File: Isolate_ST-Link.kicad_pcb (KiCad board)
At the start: 2 copper layers, 39 x 38 mm, 70 parts, among them J1 USB_OTG, J2 CONN_01X06, J3 CONN_01X04, J4 CONN_01X02, J5 CONN_01X02, J6 GS2, Q1 BSS138, U1 MAU10x, U2 ADuM4160, U3 APE8865NR-33-HF-3, U4 STM32F103CBTx, Y1 Crystal

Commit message: 進捗
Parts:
- moved R30 0.10 mm to (166.1, 75.4)
- moved R31 0.10 mm to (161.6, 75.4)
- moved R32 0.10 mm to (163.1, 75.4)
- moved R33 0.10 mm to (164.6, 75.4)
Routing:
- net GND: track 336.2 -> 383.5 mm, vias 93 -> 114
- net +3V3: track 138.4 -> 124.2 mm, vias 9 -> 8
- net /MCU/Vtarget: track 18.6 -> 20.7 mm
- net Net-(J2-Pad4): track 7.32 -> 8.08 mm
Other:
- board text added: "Vtgt"

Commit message: 進捗
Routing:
- net GND: track 383.5 -> 446.4 mm, vias 114 -> 137
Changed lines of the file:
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@@
-(kicad_pcb (version 4) (host pcbnew 4.0.7)
+(kicad_pcb (version 4) (host pcbnew 4.0.6)
   (general
     (links 148)
@@
     (thickness 1.6)
     (drawings 49)
-    (tracks 1041)
+    (tracks 1094)
     (zones 0)
     (modules 70)
@@
     (pad_to_mask_clearance 0)
     (aux_axis_origin 0 0)
-    (grid_origin 193 50)
     (visible_elements 7FFFFFFF)
     (pcbplotparams
@@
     (tags D_SOD-123F)
     (attr smd)
-    (fp_text reference D9 (at -3.3 0.1 90) (layer B.SilkS)
+    (fp_text reference D9 (at -3.2 0 90) (layer B.SilkS)
       (effects (font (size 1 1) (thickness 0.15)) (justify mirror))
     )
@@
     (tags "resistor 0603")
     (attr smd)
-    (fp_text reference R21 (at 2.6 0 180) (layer B.SilkS)
+    (fp_text reference R21 (at 0 1.4 180) (layer B.SilkS)
       (effects (font (size 1 1) (thickness 0.15)) (justify mirror))
     )
@@
     (tags "resistor 0603")
     (attr smd)
-    (fp_text reference R23 (at 0.2 -1.3 180) (layer B.SilkS)
+    (fp_text reference R23 (at -0.45 1.35 180) (layer B.SilkS)
       (effects (font (size 1 1) (thickness 0.15)) (justify mirror))
     )
@@
     (tags "resistor 0603")
     (attr smd)
-    (fp_text reference R25 (at 0 -1.4 180) (layer B.SilkS)
+    (fp_text reference R25 (at -0.15 -1.45 180) (layer B.SilkS)
       (effects (font (size 1 1) (thickness 0.15)) (justify mirror))
     )
@@
   (segment (start 163.075 60.95) (end 163.735 60.29) (width 0.6) (layer F.Cu) (net 3))
   (segment (start 163.735 60.29) (end 165.325001 60.29) (width 0.6) (layer F.Cu) (net 3))
+  (segment (start 185.8 57.3) (end 187.7 59.2) (width 0.25) (layer F.Cu) (net 4))
+  (segment (start 187.7 59.2) (end 187.8 59.2) (width 0.25) (layer F.Cu) (net 4))
+  (via (at 187.8 59.2) (size 0.6) (drill 0.4) (layers F.Cu B.Cu) (net 4))
+  (segment (start 185.8 57.3) (end 187.7 57.3) (width 0.25) (layer B.Cu) (net 4))
+  (segment (start 187.7 57.3) (end 187.8 57.2) (width 0.25) (layer B.Cu) (net 4))
+  (via (at 187.8 57.2) (size 0.6) (drill 0.4) (layers F.Cu B.Cu) (net 4))
+  (segment (start 185.8 57.3) (end 187.5 55.6) (width 0.25) (layer F.Cu) (net 4))
+  (segment (start 187.5 55.6) (end 187.8 55.6) (width 0.25) (layer F.Cu) (net 4))
+  (via (at 187.8 55.6) (size 0.6) (drill 0.4) (layers F.Cu B.Cu) (net 4))
+  (segment (start 185.8 57.3) (end 185.8 59.2) (width 0.25) (layer B.Cu) (net 4))
+  (via (at 185.8 59.2) (size 0.6) (drill 0.4) (layers F.Cu B.Cu) (net 4))
+  (segment (start 183.6 55.6) (end 181 55.6) (width 0.25) (layer F.Cu) (net 4))
+  (via (at 181 55.6) (size 0.6) (drill 0.4) (layers F.Cu B.Cu) (net 4))
+  (segment (start 185.8 57.3) (end 183.9 59.2) (width 0.25) (layer F.Cu) (net 4))
+  (segment (start 183.9 59.2) (end 183.6 59.2) (width 0.25) (layer F.Cu) (net 4))
+  (via (at 183.6 59.2) (size 0.6) (drill 0.4) (layers F.Cu B.Cu) (net 4))
+  (segment (start 185.8 57.3) (end 184.1 55.6) (width 0.25) (layer F.Cu) (net 4))
+  (segment (start 184.1 55.6) (end 183.6 55.6) (width 0.25) (layer F.Cu) (net 4))
+  (via (at 183.6 55.6) (size 0.6) (drill 0.4) (layers F.Cu B.Cu) (net 4))
+  (segment (start 157 75.4) (end 154.2 75.4) (width 0.25) (layer F.Cu) (net 4))
+  (via (at 154.2 75.4) (size 0.6) (drill 0.4) (layers F.Cu B.Cu) (net 4))
+  (segment (start 157 77.2) (end 154.2 77.2) (width 0.25) (layer B.Cu) (net 4))
+  (via (at 154.2 77.2) (size 0.6) (drill 0.4) (layers F.Cu B.Cu) (net 4))
+  (segment (start 154.2 84.8) (end 154.2 82.2) (width 0.25) (layer F.Cu) (net 4))
+  (via (at 154.2 82.2) (size 0.6) (drill 0.4) (layers F.Cu B.Cu) (net 4))
+  (segment (start 157.4 84.8) (end 154.2 84.8) (width 0.25) (layer B.Cu) (net 4))
+  (via (at 154.2 84.8) (size 0.6) (drill 0.4) (layers F.Cu B.Cu) (net 4))
+  (segment (start 157 77.2) (end 157 75.4) (width 0.25) (layer F.Cu) (net 4))
+  (via (at 157 75.4) (size 0.6) (drill 0.4) (layers F.Cu B.Cu) (net 4))
+  (segment (start 160.4 77.2) (end 157 77.2) (width 0.25) (layer B.Cu) (net 4))
+  (via (at 157 77.2) (size 0.6) (drill 0.4) (layers F.Cu B.Cu) (net 4))
+  (segment (start 157.4 84.8) (end 157.4 87.2) (width 0.25) (layer B.Cu) (net 4))
+  (via (at 157.4 87.2) (size 0.6) (drill 0.4) (layers F.Cu B.Cu) (net 4))
+  (segment (start 160 84.8) (end 157.4 84.8) (width 0.25) (layer F.Cu) (net 4))
+  (via (at 157.4 84.8) (size 0.6) (drill 0.4) (layers F.Cu B.Cu) (net 4))
+  (segment (start 162.6 87.2) (end 160 87.2) (width 0.25) (layer F.Cu) (net 4))
+  (via (at 160 87.2) (size 0.6) (drill 0.4) (layers F.Cu B.Cu) (net 4))
+  (segment (start 162.6 84.8) (end 160 84.8) (width 0.25) (layer B.Cu) (net 4))
+  (via (at 160 84.8) (size 0.6) (drill 0.4) (layers F.Cu B.Cu) (net 4))
+  (segment (start 165 87.2) (end 162.6 87.2) (width 0.25) (layer F.Cu) (net 4))
+  (via (at 162.6 87.2) (size 0.6) (drill 0.4) (layers F.Cu B.Cu) (net 4))
+  (segment (start 168.8 87.2) (end 165 87.2) (width 0.25) (layer B.Cu) (net 4))
+  (via (at 165 87.2) (size 0.6) (drill 0.4) (layers F.Cu B.Cu) (net 4))
+  (segment (start 165 84.8) (end 162.6 84.8) (width 0.25) (layer F.Cu) (net 4))
+  (via (at 162.6 84.8) (size 0.6) (drill 0.4) (layers F.Cu B.Cu) (net 4))
+  (segment (start 168.8 84.8) (end 165 84.8) (width 0.25) (layer B.Cu) (net 4))
+  (via (at 165 84.8) (size 0.6) (drill 0.4) (layers F.Cu B.Cu) (net 4))
+  (segment (start 181.4 66.6) (end 181.4 67.3) (width 0.25) (layer B.Cu) (net 4))
+  (segment (start 181.4 67.3) (end 180.5 68.2) (width 0.25) (layer B.Cu) (net 4))
+  (segment (start 181.4 63.9) (end 181.4 66.6) (width 0.25) (layer F.Cu) (net 4))
+  (via (at 181.4 66.6) (size 0.6) (drill 0.4) (layers F.Cu B.Cu) (net 4))
+  (via (at 180.5 68.2) (size 0.6) (drill 0.4) (layers F.Cu B.Cu) (net 4))
+  (segment (start 184.2 65) (end 182.5 65) (width 0.25) (layer F.Cu) (net 4))
+  (segment (start 182.5 65) (end 181.4 63.9) (width 0.25) (layer F.Cu) (net 4))
+  (via (at 181.4 63.9) (size 0.6) (drill 0.4) (layers F.Cu B.Cu) (net 4))
   (segment (start 172.65 69.45) (end 172.65 70.05) (width 0.25) (layer F.Cu) (net 4))
   (segment (start 172.65 70.05) (end 172.69999 70.09999) (width 0.25) (layer F.Cu) (net 4))
@@
   (segment (start 154.399999 73.081803) (end 154.399999 75.7) (width 0.25) (layer B.Cu) (net 4))
   (segment (start 185.8 57.3) (end 185.7 57.3) (width 0.25) (layer B.Cu) (net 4))
-  (segment (start 185.7 57.3) (end 184.2 58.8) (width 0.25) (layer B.Cu) (net 4))
-  (via (at 184.2 58.8) (size 0.6) (drill 0.4) (layers F.Cu B.Cu) (net 4))
   (segment (start 185.8 57.3) (end 183.6 57.3) (width 0.6) (layer F.Cu) (net 4))
   (segment (start 183.6 57.3) (end 181.8 57.3) (width 0.6) (layer F.Cu) (net 4))
@@
     (connect_pads (clearance 0.254))
     (min_thickness 0.254)
-    (fill (arc_segments 16) (thermal_gap 0.508) (thermal_bridge_width 0.508))
+    (fill yes (arc_segments 16) (thermal_gap 0.508) (thermal_bridge_width 0.508))
     (polygon
       (pts
@@
     (connect_pads (clearance 0.254))
     (min_thickness 0.254)
-    (fill (arc_segments 16) (thermal_gap 0.508) (thermal_bridge_width 0.508))
+    (fill yes (arc_segments 16) (thermal_gap 0.508) (thermal_bridge_width 0.508))
     (polygon
       (pts
@@
     (connect_pads (clearance 0.254))
     (min_thickness 0.254)
-    (fill (arc_segments 16) (thermal_gap 0.254) (thermal_bridge_width 0.508))
+    (fill yes (arc_segments 16) (thermal_gap 0.254) (thermal_bridge_width 0.508))
     (polygon
       (pts
@@
     (connect_pads (clearance 0.254))
     (min_thickness 0.254)
-    (fill (arc_segments 16) (thermal_gap 0.254) (thermal_bridge_width 0.508))
+    (fill yes (arc_segments 16) (thermal_gap 0.254) (thermal_bridge_width 0.508))
     (polygon
       (pts
@@
     (min_thickness 0.254)
     (keepout (tracks not_allowed) (vias not_allowed) (copperpour not_allowed))
-    (fill (arc_segments 16) (thermal_gap 0.508) (thermal_bridge_width 0.508))
+    (fill yes (arc_segments 16) (thermal_gap 0.508) (thermal_bridge_width 0.508))
     (polygon
       (pts

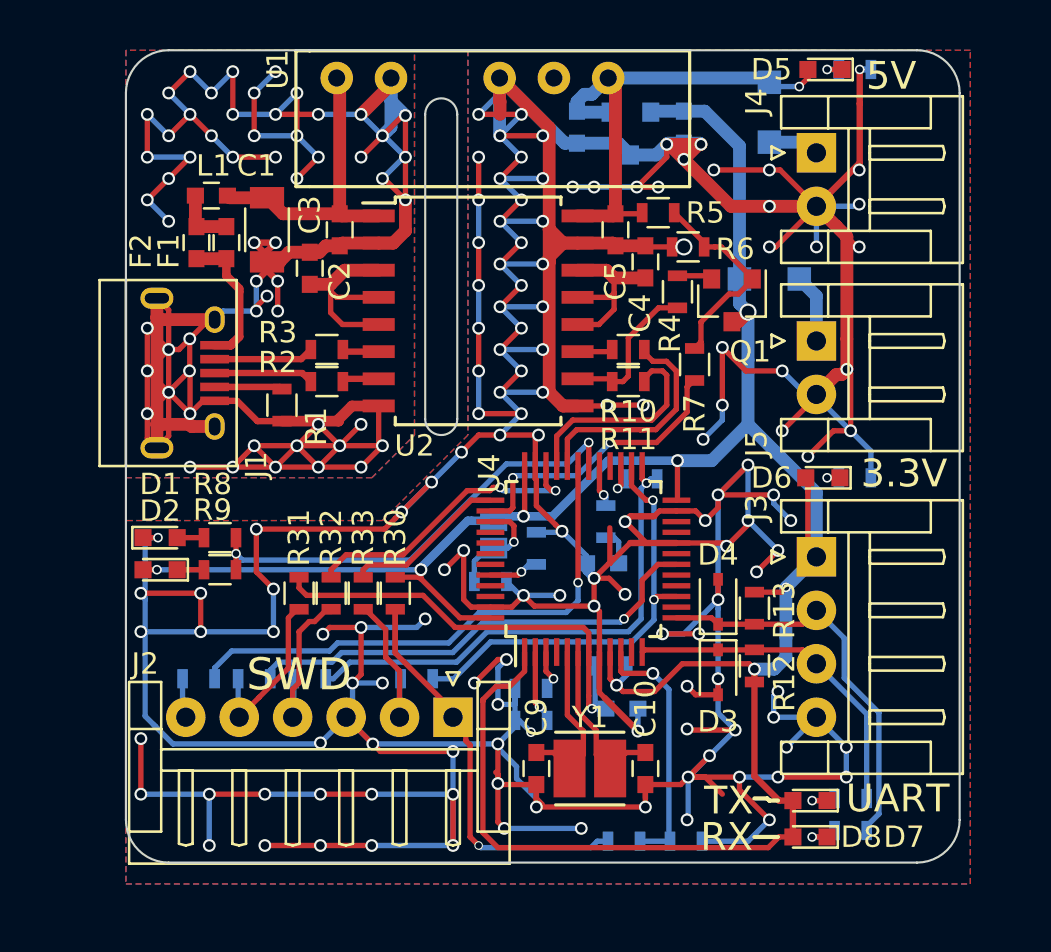
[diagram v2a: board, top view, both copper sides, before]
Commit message: UARTのシルクの位置を修正
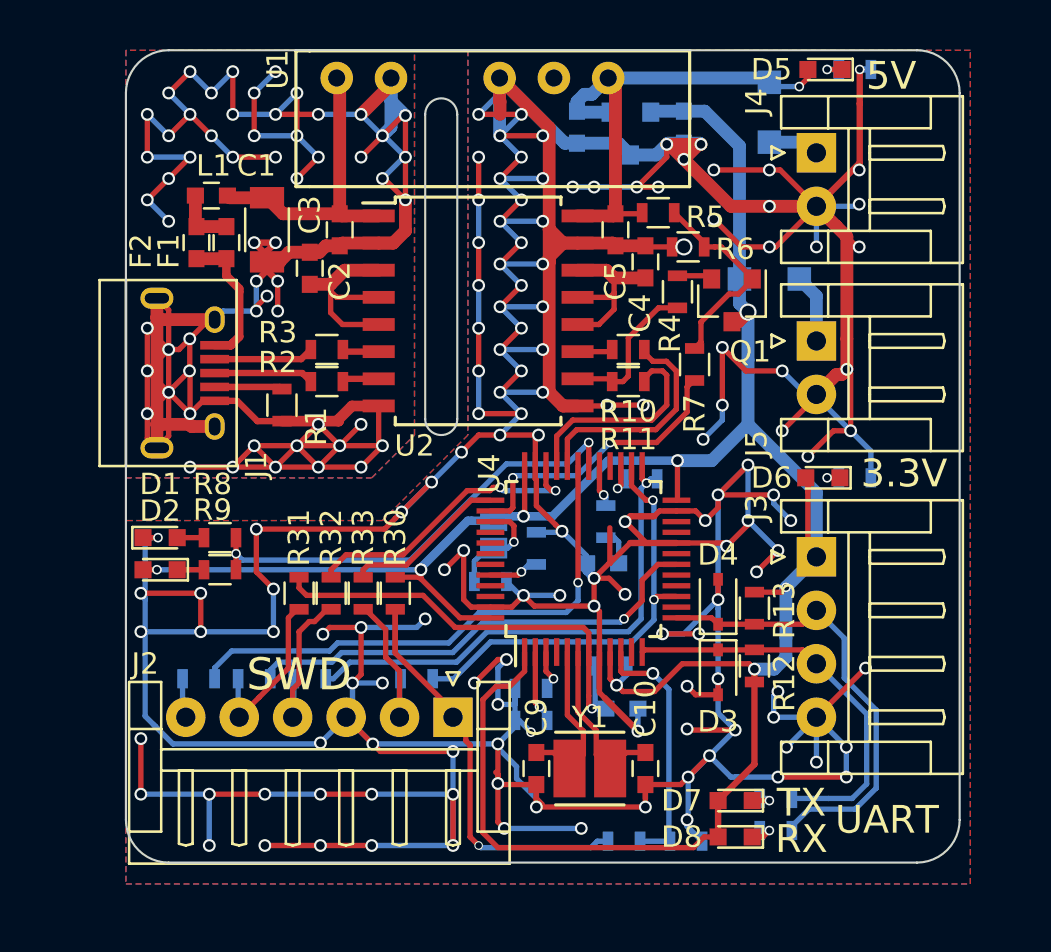
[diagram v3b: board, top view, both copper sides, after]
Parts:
- moved D7 3.50 mm to (182.0, 85.1)
- moved D8 3.50 mm to (182.0, 86.8)
- moved R19 3.50 mm to (183.9, 85.0)
- moved R20 3.50 mm to (183.9, 86.5)
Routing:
- net +3V3: track 124.2 -> 120.3 mm
- net /MCU/UART_TX: track 16.5 -> 19.6 mm
- net /MCU/UART_RX: track 18.7 -> 21.3 mm
- net GND: track 446.4 -> 447.7 mm, vias 137 -> 138
- net Net-(D8-Pad1): track 1.87 -> 1.37 mm

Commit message: MicroUSBの位置を少しずらした
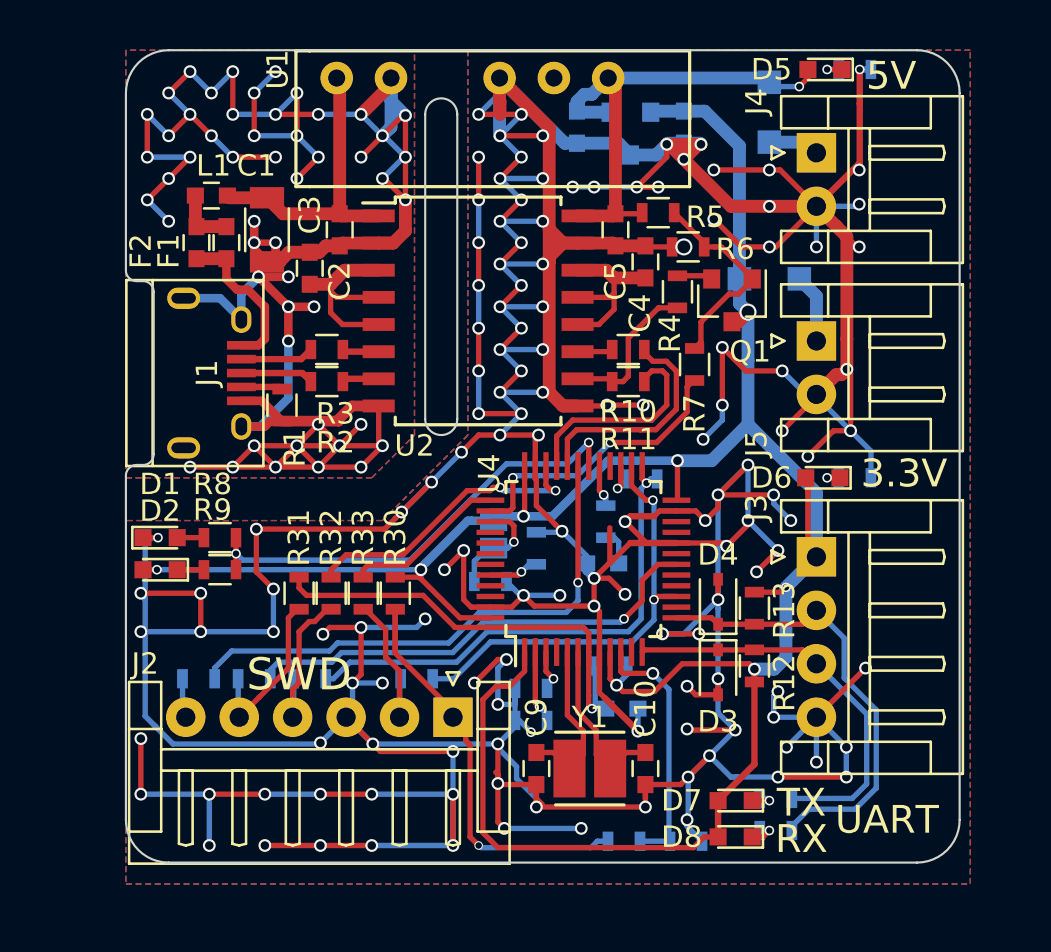
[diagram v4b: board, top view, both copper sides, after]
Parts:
- moved J1 1.25 mm to (157.6, 65.1)
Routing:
- net GNDPWR: track 161.1 -> 129.7 mm, vias 58 -> 51
- net Net-(J1-Pad4): track 3.19 -> 1.94 mm
- net Net-(J1-Pad2): track 4.69 -> 3.44 mm
- net Net-(J1-Pad3): track 4.67 -> 3.42 mm
- net Net-(F1-Pad2): track 6.79 -> 7.41 mm
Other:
- outline, holes or cut-outs redrawn
- net class Default: clearance 0.2 -> 0.199
- rule trace_clearance: 0.2 -> 0.199
- rule trace_min: 0.1999 -> 0.2

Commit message: Kicad5.0用に更新，フットプリント変わったのでDRC引っかかりまくった
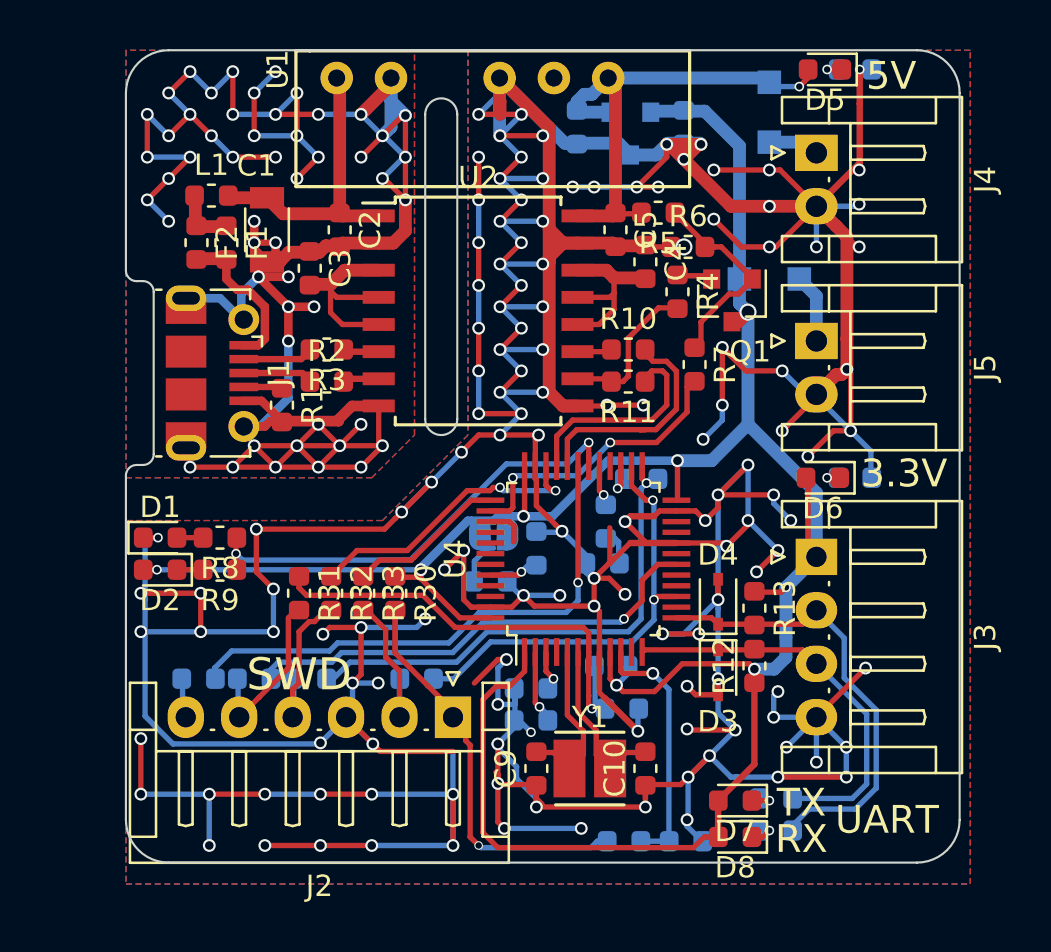
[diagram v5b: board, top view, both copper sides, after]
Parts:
- C1: value 47u -> 10u
- C10, C11, C2, C3, C4, C5, C6, C7, C8, C9: footprint Capacitors_SMD:C_0603 -> Capacitor_SMD:C_0603_1608Metric
- D1, D2, D5, D6, D7, D8: footprint LEDs:LED_0603 -> LED_SMD:LED_0603_1608Metric
- D10, D9: footprint Diodes_SMD:D_SOD-123F -> Diode_SMD:D_SOD-123F
- D3, D4: footprint Diodes_SMD:D_SOD-323 -> Diode_SMD:D_SOD-323
- F1, F2: footprint Capacitors_SMD:C_0603 -> Fuse:Fuse_0603_1608Metric
- J1: footprint Connectors:USB_Micro-B -> Connector_USB:USB_Micro-B_Molex-105017-0001
- J2: footprint Connectors_JST:JST_EH_S06B-EH_06x2.50mm_Angled -> Connector_JST:JST_EH_S06B-EH_1x06_P2.50mm_Horizontal
- J3: footprint Connectors_JST:JST_EH_S04B-EH_04x2.50mm_Angled -> Connector_JST:JST_EH_S04B-EH_1x04_P2.50mm_Horizontal
- J4, J5: footprint Connectors_JST:JST_EH_S02B-EH_02x2.50mm_Angled -> Connector_JST:JST_EH_S02B-EH_1x02_P2.50mm_Horizontal
- J6: footprint Connectors:GS2 -> Jumper:SolderJumper-2_P1.3mm_Open_RoundedPad1.0x1.5mm
- L1: footprint Capacitors_SMD:C_0603 -> Inductor_SMD:L_0603_1608Metric
- Q1, U3: footprint TO_SOT_Packages_SMD:SOT-23 -> Package_TO_SOT_SMD:SOT-23
- R1, R10, R11, R12, R13, R14, R15, R16, R17, R18, R19, R2, R20, R21, R22, R23, R24, R25, R26, R27, R28, R29, R3, R30, R31, R32, R33, R34, R4, R5, R6, R7, R8, R9: footprint Resistors_SMD:R_0603 -> Resistor_SMD:R_0603_1608Metric
- U1: footprint Converters_DCDC_ACDC:DCDC-Conv_Minimax_MAU10x -> Converter_DCDC(my):DCDC-Conv_Minimax_MAU10x
- U2: footprint Housings_SOIC:SOIC-16W_7.5x10.3mm_Pitch1.27mm -> Package_SO:SOIC-16W_7.5x10.3mm_P1.27mm
- U4: footprint Housings_QFP:LQFP-48_7x7mm_Pitch0.5mm -> Package_QFP:LQFP-48_7x7mm_P0.5mm
- Y1: footprint Crystals:NDK_Crystal_SMD_3225_2Pads -> Crystal(my):NDK_Crystal_SMD_3225_2Pads
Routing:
- net GND: track 447.7 -> 441.8 mm, vias 138 -> 136
- net Net-(J6-Pad1): track 5.52 -> 4.04 mm, vias 1 -> 0
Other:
- rule trace_min: 0.2 -> 0.199

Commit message: DRC全部パスした
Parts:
- moved C11 1.40 mm to (175.8, 75.4)
- moved R26 1.35 mm to (176.8, 73.1)
- moved R1 1.26 mm to (162.0, 67.0), turned to 0 degrees
- moved R14 1.10 mm to (163.2, 79.4)
- moved R6 0.90 mm to (180.7, 59.2)
- moved R15 0.70 mm to (160.2, 79.4)
- moved R24 0.61 mm to (173.3, 73.2)
- moved J6 0.50 mm to (171.2, 72.7)
- moved R34 0.45 mm to (170.6, 74.4)
- moved R16 0.30 mm to (157.2, 79.4)
- moved R12 0.16 mm to (182.9, 79.0)
- moved R13 0.10 mm to (182.9, 76.0)
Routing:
- net GND: track 441.8 -> 412.9 mm, vias 136 -> 124
- net GNDPWR: track 129.7 -> 113.8 mm, vias 51 -> 50
- net Net-(J1-Pad2): track 3.44 -> 6.72 mm
- net Net-(J1-Pad3): track 3.42 -> 6.68 mm
- net +3V3: track 120.3 -> 122.6 mm
- net Net-(R26-Pad1): track 1.97 -> 3.43 mm
- net T_SWO: track 25.1 -> 26.3 mm
- net Net-(R22-Pad2): track 1.71 -> 2.78 mm
- net Net-(J6-Pad1): track 4.04 -> 5.05 mm, vias 0 -> 1
- net T_NRST: track 22.0 -> 21.0 mm
- net T_JTMS: track 23.9 -> 22.9 mm
- net Net-(J1-Pad4): track 1.94 -> 2.72 mm
- net Net-(R24-Pad1): track 2.36 -> 2.98 mm
- net SYS_JTMS: track 14.1 -> 13.5 mm

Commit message: 10pin版つくった
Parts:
- J2: value CONN_01X06 -> Conn_02x05_Odd_Even; footprint Connector_JST:JST_EH_S06B-EH_1x06_P2.50mm_Horizontal -> Connector_PinHeader_1.27mm:PinHeader_2x05_P1.27mm_Vertical_SMD
- moved J2 6.84 mm to (162.4, 83.6), turned to 90 degrees
- moved R16 6.24 mm to (163.4, 80.1), turned to 90 degrees
- moved R15 4.75 mm to (164.9, 80.1), turned to 90 degrees
- moved R31 3.72 mm to (164.6, 77.6)
- moved R14 3.30 mm to (166.4, 80.2), turned to 90 degrees
- moved R33 2.66 mm to (163.1, 77.6)
- moved R32 2.65 mm to (161.6, 77.6)
- moved R30 2.20 mm to (166.1, 77.6)
- moved R28 1.13 mm to (167.9, 80.2), turned to 270 degrees
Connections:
- J2 pad 5: Net-(J2-Pad5) -> GND
- R14 pad 1: Net-(J2-Pad4) -> Net-(J2-Pad2)
- R15 pad 1: Net-(J2-Pad5) -> Net-(J2-Pad10)
- R28 pad 2: Net-(J2-Pad2) -> Net-(J2-Pad4)
- R31 pad 2: Net-(J2-Pad5) -> Net-(J2-Pad10)
- R32 pad 2: Net-(J2-Pad4) -> Net-(J2-Pad2)
- R33 pad 2: Net-(J2-Pad2) -> Net-(J2-Pad4)
- U1 pad 5: Net-(U1-Pad5) -> (no net)
- U4 pad 11: Net-(U4-Pad11) -> (no net)
- U4 pad 14: Net-(U4-Pad14) -> (no net)
- U4 pad 16: T_JTDO -> (no net)
- U4 pad 17: T_JTDI -> (no net)
- U4 pad 19: Net-(U4-Pad19) -> (no net)
- U4 pad 21: Net-(U4-Pad21) -> (no net)
- U4 pad 22: Net-(U4-Pad22) -> (no net)
- U4 pad 28: Net-(U4-Pad28) -> (no net)
- U4 pad 4: Net-(U4-Pad4) -> (no net)
- U4 pad 40: Net-(U4-Pad40) -> (no net)
- U4 pad 41: Net-(U4-Pad41) -> (no net)
- U4 pad 42: Net-(U4-Pad42) -> (no net)
- U4 pad 43: Net-(U4-Pad43) -> (no net)
- U4 pad 45: Net-(U4-Pad45) -> (no net)
- U4 pad 46: Net-(U4-Pad46) -> (no net)
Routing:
- net GND: track 412.9 -> 351.7 mm, vias 124 -> 120
- net /MCU/Vtarget: track 20.7 -> 30.4 mm, vias 1 -> 2
- net Net-(J2-Pad5): track 8.95 -> 0.00 mm
- net T_SWO: track 26.3 -> 20.8 mm
- net Net-(J2-Pad4): track 8.36 -> 12.8 mm, vias 0 -> 1
- net Net-(J2-Pad10): track 0.00 -> 4.11 mm, vias 0 -> 1
- net T_NRST: track 21.0 -> 17.1 mm
- net SYS_NRST: track 21.2 -> 17.5 mm
- net SYS_JTCK: track 7.78 -> 11.1 mm
- net Net-(J2-Pad2): track 7.66 -> 11.0 mm, vias 0 -> 1
- net SYS_JTMS: track 13.5 -> 16.8 mm
- net T_JTMS: track 22.9 -> 20.5 mm
- net +3V3: track 122.6 -> 124.3 mm
- net Net-(J2-Pad6): track 2.06 -> 2.35 mm, vias 0 -> 1
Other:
- board text removed: "NRST"
- board text removed: "SWCLK"
- board text removed: "SWDIO"
- board text removed: "SWO"
- board text removed: "Vtgt"
